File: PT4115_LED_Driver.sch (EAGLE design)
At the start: 57 parts, among them IC1 PCA9685PW, IC2 TMP421

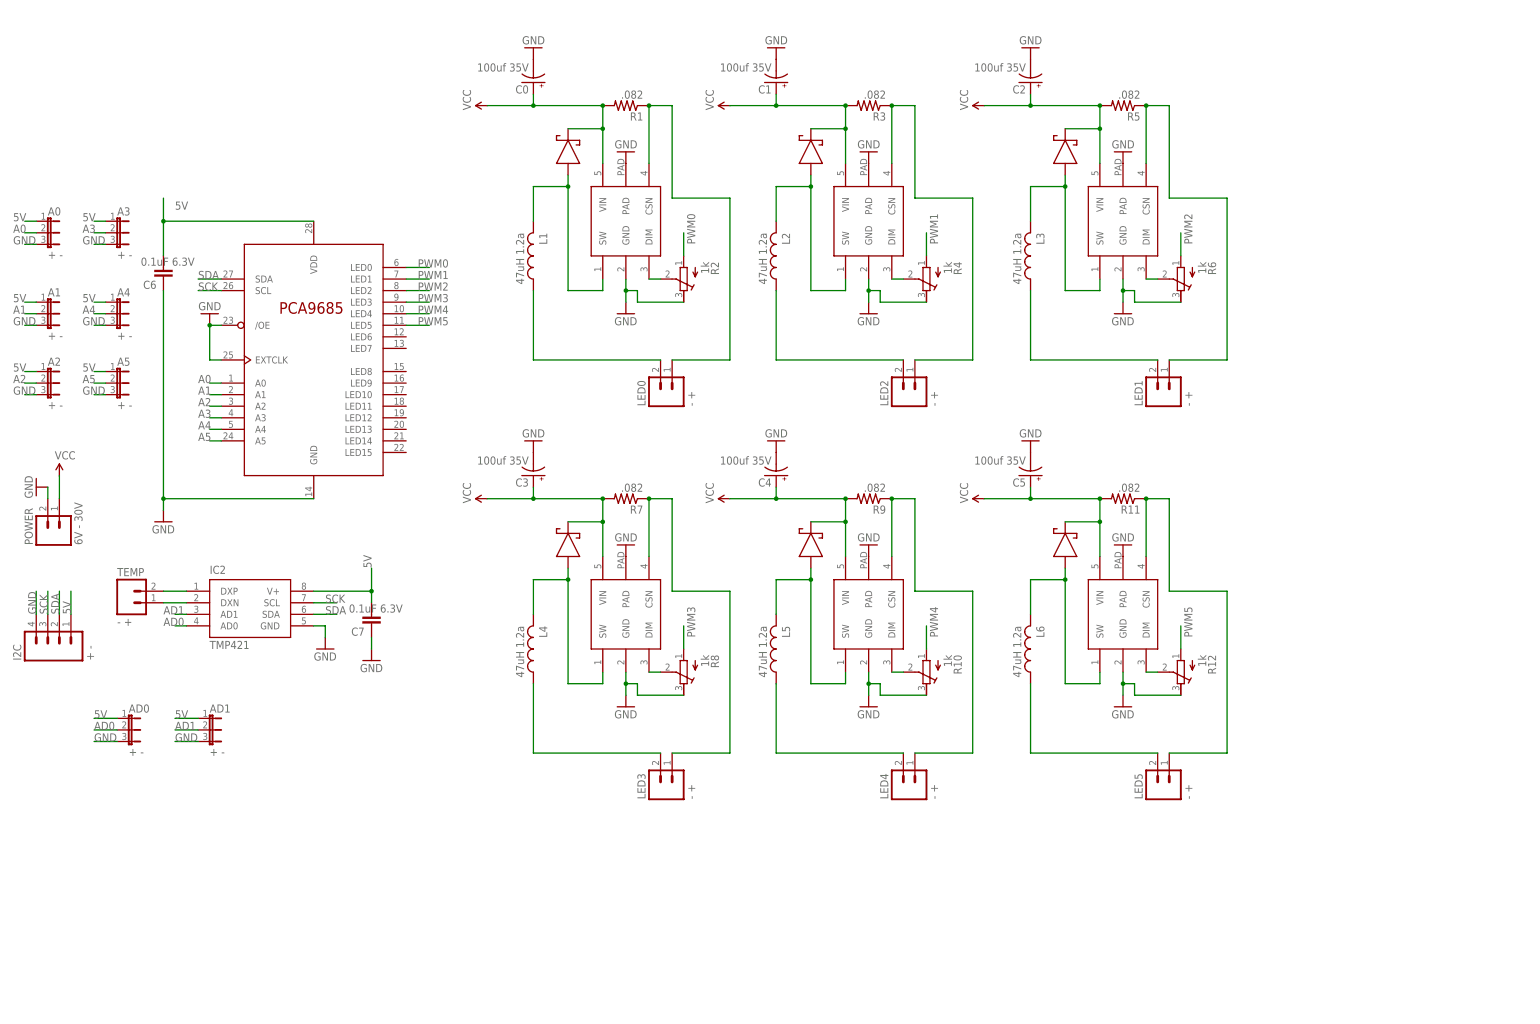
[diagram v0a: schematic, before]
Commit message: Simplified some routes.  Cleaned up ground and 5v planes.  Added img exports.
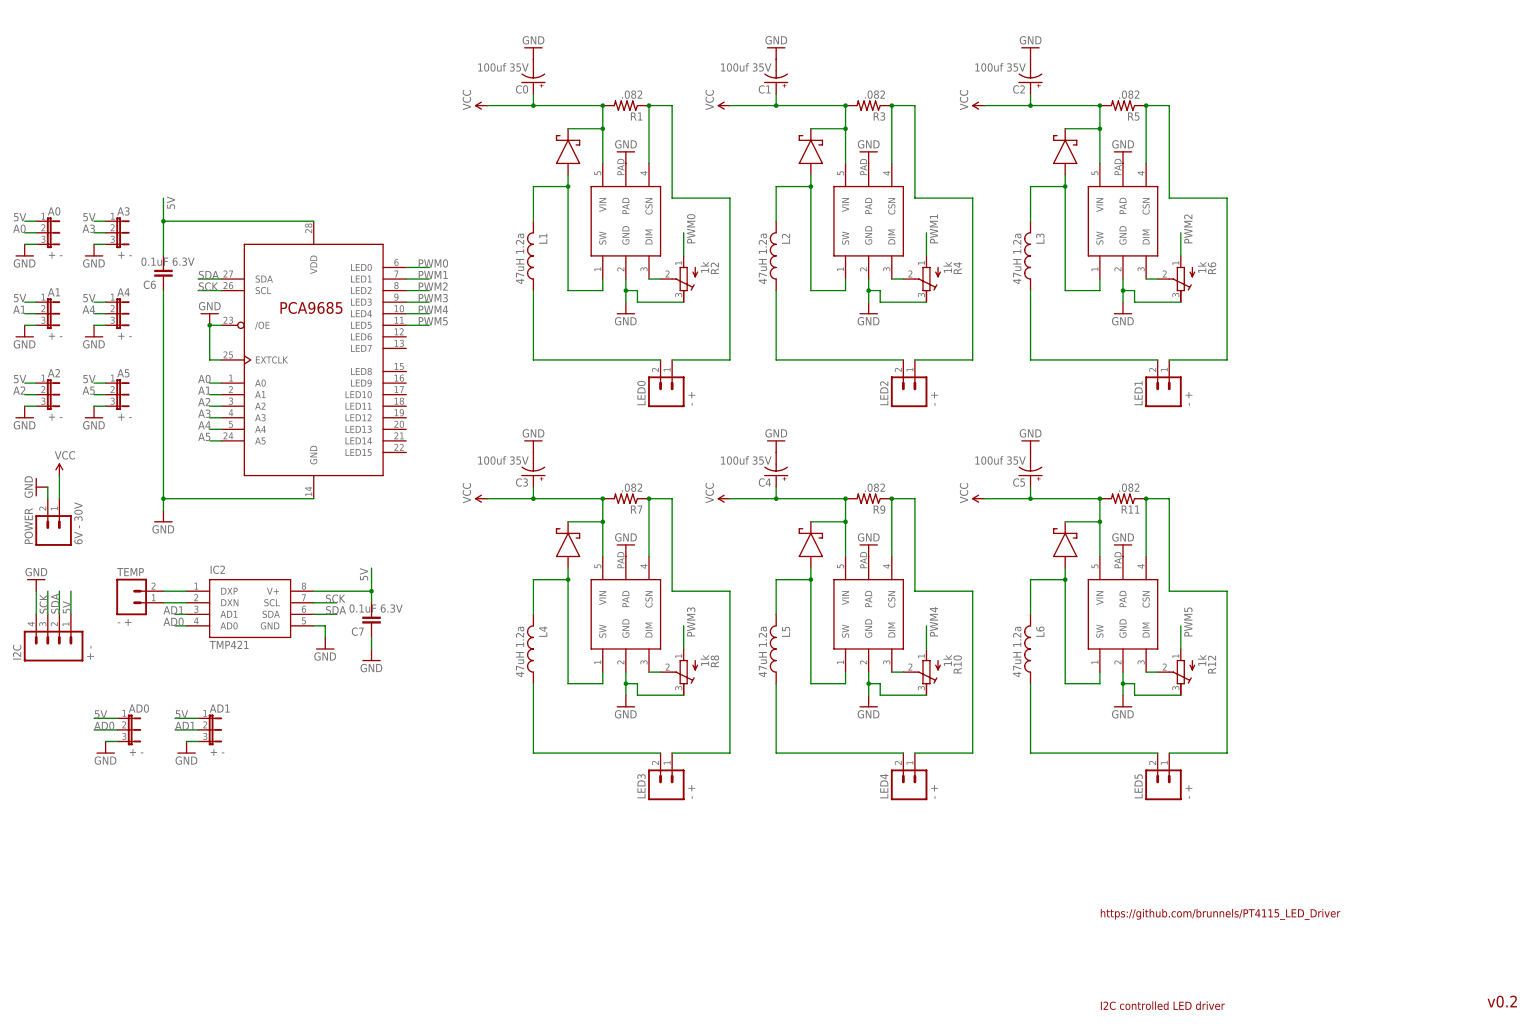
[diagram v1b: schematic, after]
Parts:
- C6, C7: device SparkFun:CAP0603-CAP -> SparkFun:CAP0805
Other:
- note added: "I2C controlled LED driver"
- note added: "https://github.com/brunnels/PT4115_LED_Driver"
- note added: "v0.2"
- moved on the sheet: A2, A5

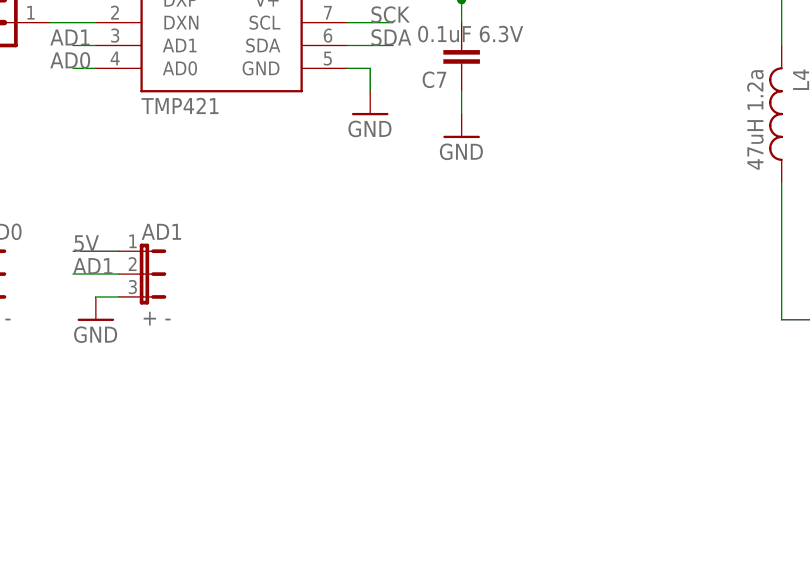
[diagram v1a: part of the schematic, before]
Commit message: Added led 5v power indicator
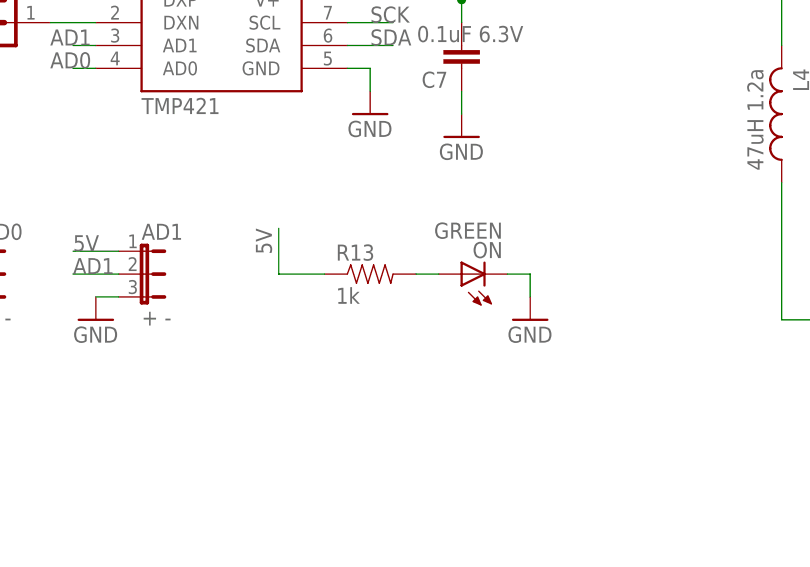
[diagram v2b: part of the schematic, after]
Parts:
- added ON: GREEN, led:LEDCHIPLED_0603
- added R13: 1k, SparkFun:RESISTOR0603-RES
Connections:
- new net N$30: ON.A, R13.2
- net 5V: now also R13.1
- net GND: now also ON.C
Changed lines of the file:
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@@
 <part name="GND31" library="supply1" deviceset="GND" device=""/>
 <part name="GND32" library="supply1" deviceset="GND" device=""/>
+<part name="R13" library="SparkFun" deviceset="RESISTOR" device="0603-RES" value="1k"/>
+<part name="ON" library="led" deviceset="LED" device="CHIPLED_0603" value="GREEN"/>
+<part name="GND33" library="supply1" deviceset="GND" device=""/>
 </parts>
 <sheets>
@@
 <instance part="GND31" gate="1" x="-40.64" y="-33.02"/>
 <instance part="GND32" gate="1" x="-58.42" y="-33.02"/>
+<instance part="R13" gate="G$1" x="-10.16" y="-27.94"/>
+<instance part="ON" gate="G$1" x="0" y="-27.94" rot="R90"/>
+<instance part="GND33" gate="1" x="7.62" y="-33.02"/>
 </instances>
 <busses>
@@
 <wire x1="0" y1="-7.62" x2="0" y2="-10.16" width="0.1524" layer="91"/>
 </segment>
+<segment>
+<pinref part="ON" gate="G$1" pin="C"/>
+<pinref part="GND33" gate="1" pin="GND"/>
+<wire x1="5.08" y1="-27.94" x2="7.62" y2="-27.94" width="0.1524" layer="91"/>
+<wire x1="7.62" y1="-27.94" x2="7.62" y2="-30.48" width="0.1524" layer="91"/>
+</segment>
 </net>
 <net name="5V" class="0">
@@
 <wire x1="-66.04" y1="-2.54" x2="-66.04" y2="2.54" width="0.1524" layer="91"/>
 <label x="-66.04" y="-2.54" size="1.778" layer="95" rot="R90"/>
+</segment>
+<segment>
+<pinref part="R13" gate="G$1" pin="1"/>
+<wire x1="-15.24" y1="-27.94" x2="-20.32" y2="-27.94" width="0.1524" layer="91"/>
+<wire x1="-20.32" y1="-27.94" x2="-20.32" y2="-22.86" width="0.1524" layer="91"/>
+<label x="-22.86" y="-22.86" size="1.778" layer="95" rot="R270"/>
 </segment>
 </net>
@@
 </segment>
 </net>
+<net name="N$30" class="0">
+<segment>
+<pinref part="R13" gate="G$1" pin="2"/>
+<pinref part="ON" gate="G$1" pin="A"/>
+<wire x1="-5.08" y1="-27.94" x2="-2.54" y2="-27.94" width="0.1524" layer="91"/>
+</segment>
+</net>

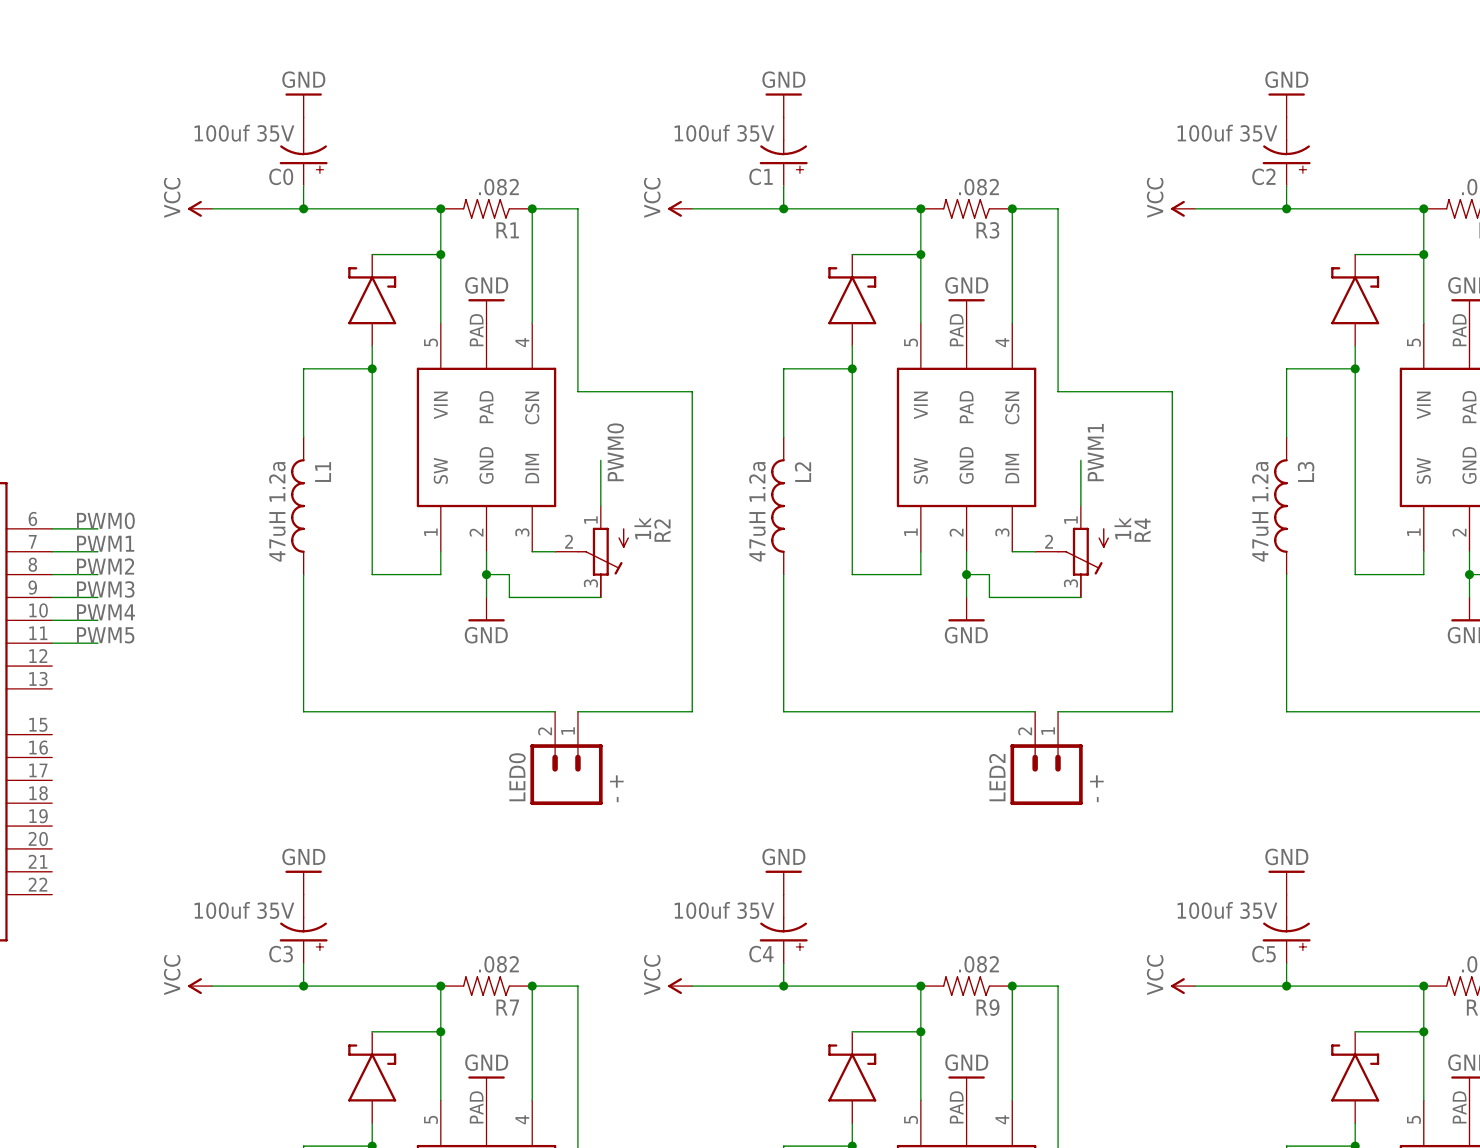
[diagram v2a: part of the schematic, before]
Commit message: Switched to larger Panasinonic F size capacitors for low ESR part availability.
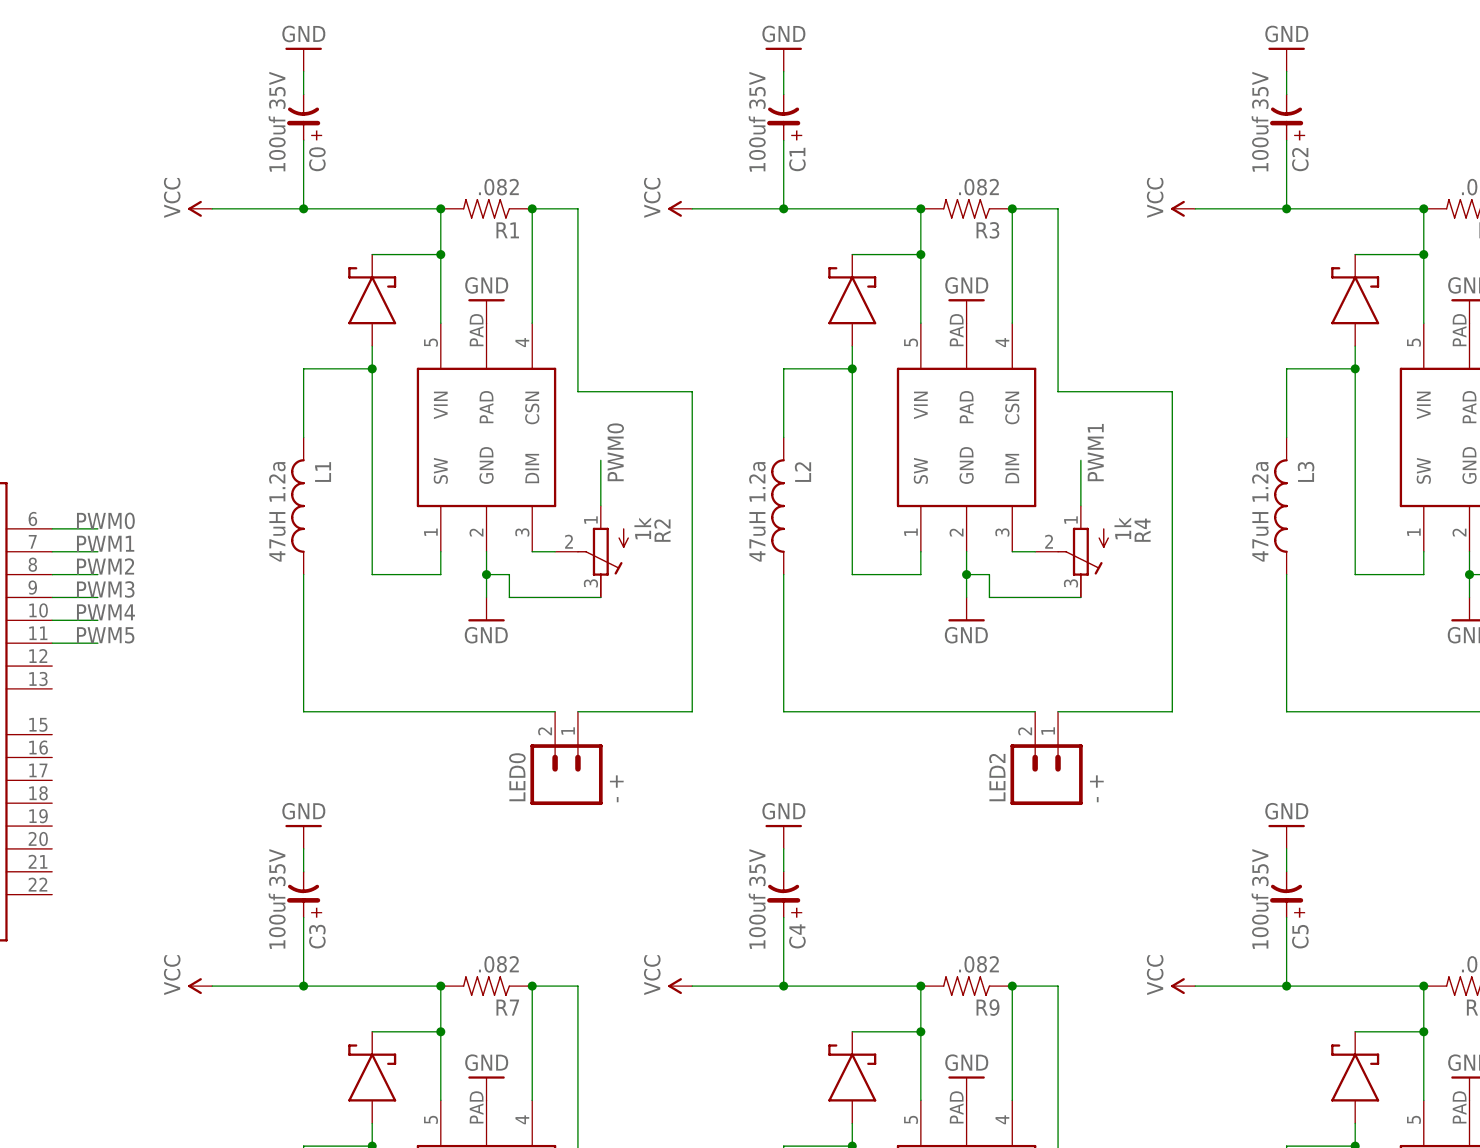
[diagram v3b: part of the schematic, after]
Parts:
- C0, C1, C2, C3, C4, C5: device SparkFun:CAP_POLD -> rc-master:CP_SV-E/F
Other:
- moved on the sheet: C0, C1, C2, C3, C4, C5
